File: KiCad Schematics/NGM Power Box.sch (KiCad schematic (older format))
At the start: 2 parts

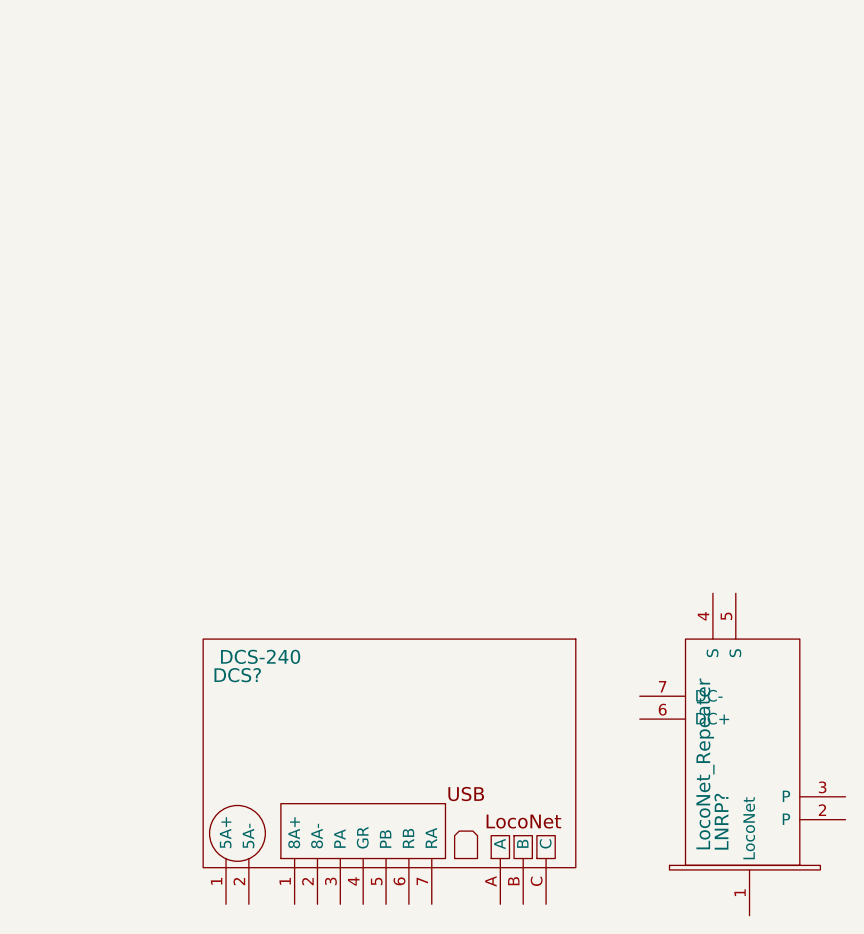
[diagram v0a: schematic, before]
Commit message: Updated schematic
Reorganized folder and updated the schematic to include multiple sheets.
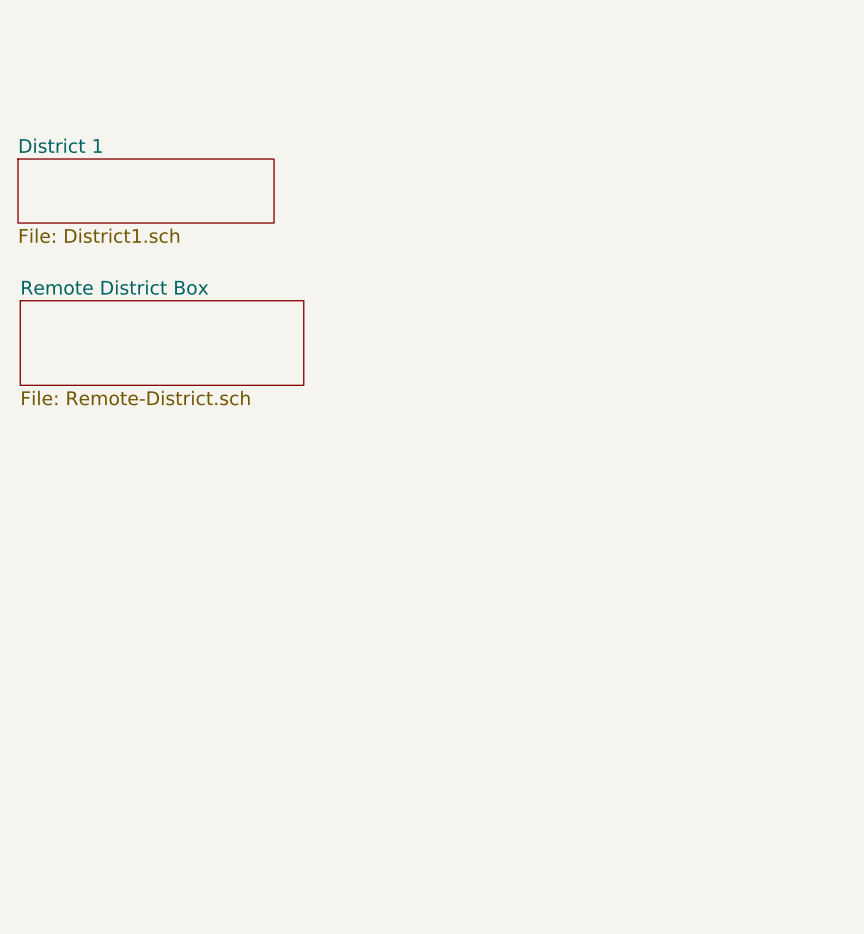
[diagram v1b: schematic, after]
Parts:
- removed DCS?: DCS-240, symbol DCS-240
- removed LNRP?: LocoNet_Repeater, symbol LocoNet_Repeater
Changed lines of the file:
@@
 EESchema Schematic File Version 2
+LIBS:NGM Power Box-rescue
 LIBS:power
 LIBS:device
@@
 LIBS:ngm_components
 LIBS:Symbols_Transformer-Diskrete_RevA
+LIBS:m-junction_box
+LIBS:NGM-Custom
+LIBS:relay_3pdt
+LIBS:NGM Power Box-cache
 EELAYER 25 0
 EELAYER END
-$Descr A4 11693 8268
+$Descr USLetter 11000 8500
 encoding utf-8
-Sheet 1 1
-Title ""
-Date ""
+Sheet 1 3
+Title "NGM Power and LocoNet Power Boxes"
+Date "2016-08-27"
 Rev ""
-Comp ""
+Comp "North Georgia Modurail"
 Comment1 ""
 Comment2 ""
@@
 Comment4 ""
 $EndDescr
-$Comp
-L DCS-240 DCS?
-U 1 1 57ACF629
-P 2100 4680
-F 0 "DCS?" H 2250 5520 60  0000 C CNN
-F 1 "DCS-240" H 2350 5600 60  0000 C CNN
-F 2 "" H 2090 4880 60  0000 C CNN
-F 3 "" H 2090 4880 60  0000 C CNN
-	1    2100 4680
-	1    0    0    -1
-$EndComp
-$Comp
-L LocoNet_Repeater LNRP?
-U 1 1 57ACF698
-P 4710 4670
-F 0 "LNRP?" H 4900 5010 60  0000 C CNN
-F 1 "LocoNet_Repeater" H 5150 5090 60  0000 C CNN
-F 2 "" H 4800 4900 60  0000 C CNN
-F 3 "" H 4800 4900 60  0000 C CNN
-	1    4710 4670
-	0    -1   -1   0
-$EndComp
+$Sheet
+S 1290 1580 1120 280
+U 57C1C4BF
+F0 "District 1" 60
+F1 "District1.sch" 60
+$EndSheet
+$Sheet
+S 1300 2200 1240 370
+U 57C1C56F
+F0 "Remote District Box" 60
+F1 "Remote-District.sch" 60
+$EndSheet
 $EndSCHEMATC

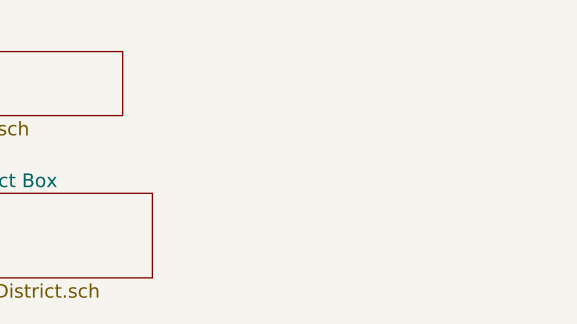
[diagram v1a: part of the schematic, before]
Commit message: Updated schematics
Fixed wiring using the correct pin-outs for the Triad transformers. Made
other minor changes.
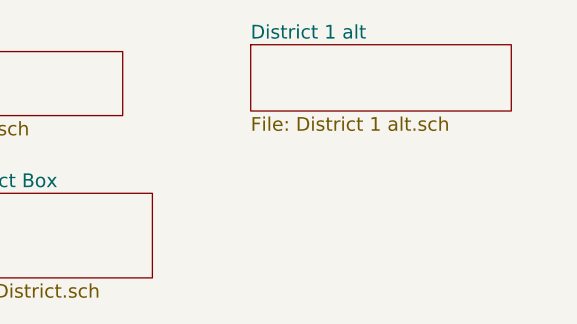
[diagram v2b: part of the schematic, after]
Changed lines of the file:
@@
 $Descr USLetter 11000 8500
 encoding utf-8
-Sheet 1 3
+Sheet 1 4
 Title "NGM Power and LocoNet Power Boxes"
 Date "2016-08-27"
-Rev ""
+Rev "2"
 Comp "North Georgia Modurail"
 Comment1 ""
@@
 F1 "Remote-District.sch" 60
 $EndSheet
+$Sheet
+S 2970 1550 1140 290
+U 57E26D35
+F0 "District 1 alt" 60
+F1 "District 1 alt.sch" 60
+$EndSheet
 $EndSCHEMATC

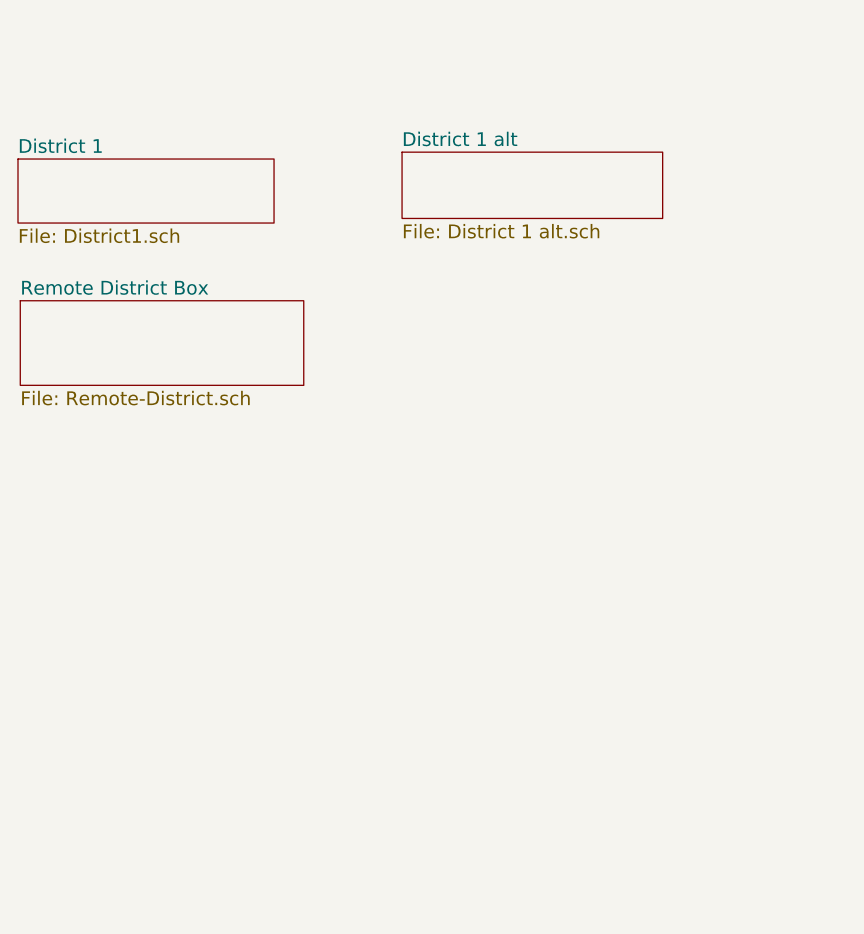
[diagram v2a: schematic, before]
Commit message: Updated schematic to include extra sheets.
Added several alternate wiring sheets and made some changes to the
schematic to reflect team decision. More to come.
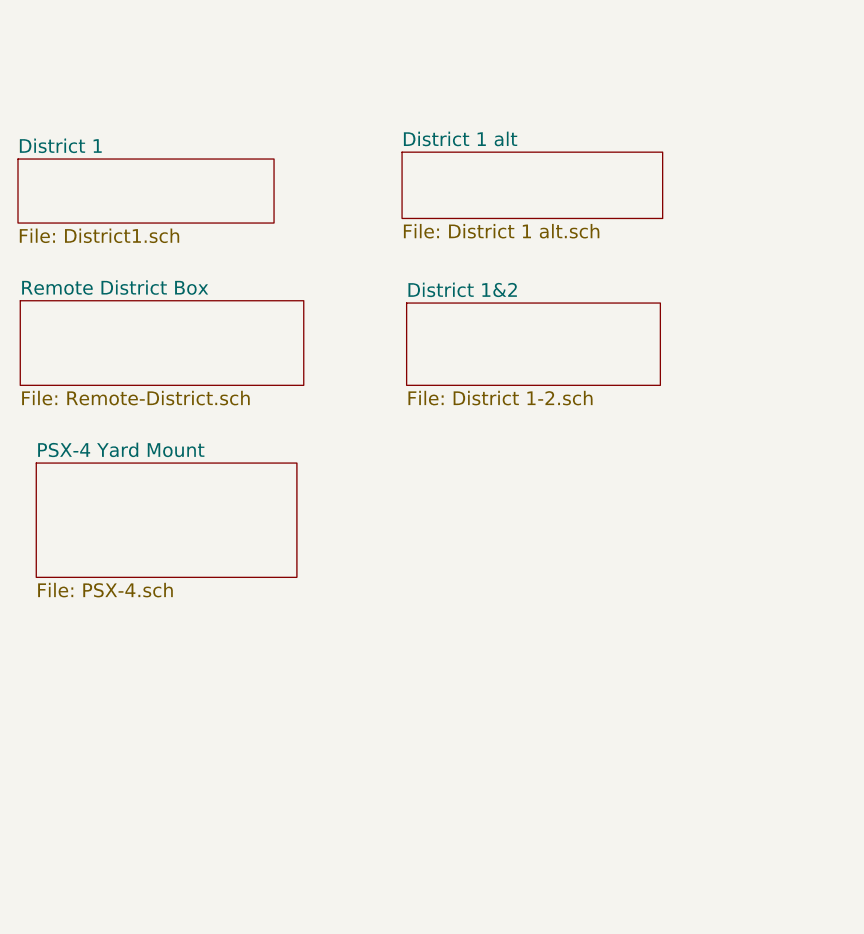
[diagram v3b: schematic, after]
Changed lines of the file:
@@
 $Descr USLetter 11000 8500
 encoding utf-8
-Sheet 1 4
+Sheet 1 6
 Title "NGM Power and LocoNet Power Boxes"
-Date "2016-08-27"
-Rev "2"
+Date "2016-09-30"
+Rev "4"
 Comp "North Georgia Modurail"
 Comment1 ""
@@
 F1 "District 1 alt.sch" 60
 $EndSheet
+$Sheet
+S 2990 2210 1110 360
+U 57EBE249
+F0 "District 1&2" 60
+F1 "District 1-2.sch" 60
+$EndSheet
+$Sheet
+S 1370 2910 1140 500
+U 57EED52C
+F0 "PSX-4 Yard Mount" 60
+F1 "PSX-4.sch" 60
+$EndSheet
 $EndSCHEMATC

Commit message: Updated schematic
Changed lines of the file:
@@
 $Descr USLetter 11000 8500
 encoding utf-8
-Sheet 1 6
+Sheet 1 7
 Title "NGM Power and LocoNet Power Boxes"
 Date "2016-09-30"
@@
 F1 "PSX-4.sch" 60
 $EndSheet
+$Sheet
+S 3220 2980 1100 390
+U 57F1B72E
+F0 "Power Box Final" 60
+F1 "Main Power Box.sch" 60
+$EndSheet
 $EndSCHEMATC

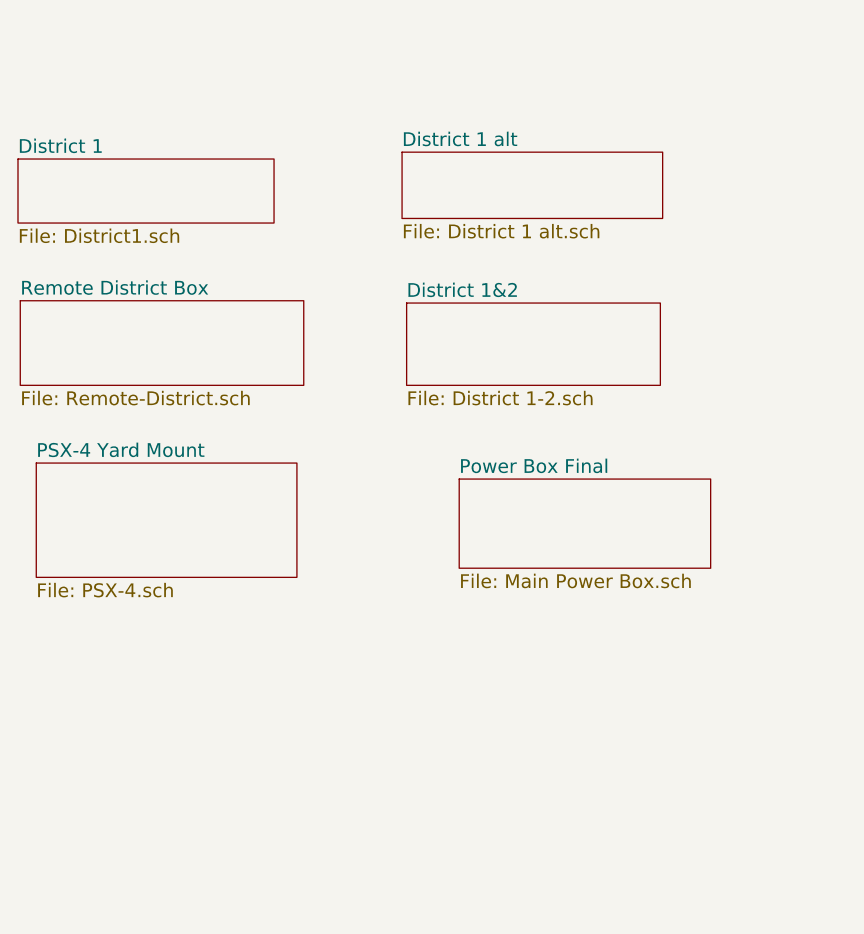
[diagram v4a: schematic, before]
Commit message: Simplified schematic
Added heirarchy sheets to simplify the schematic.
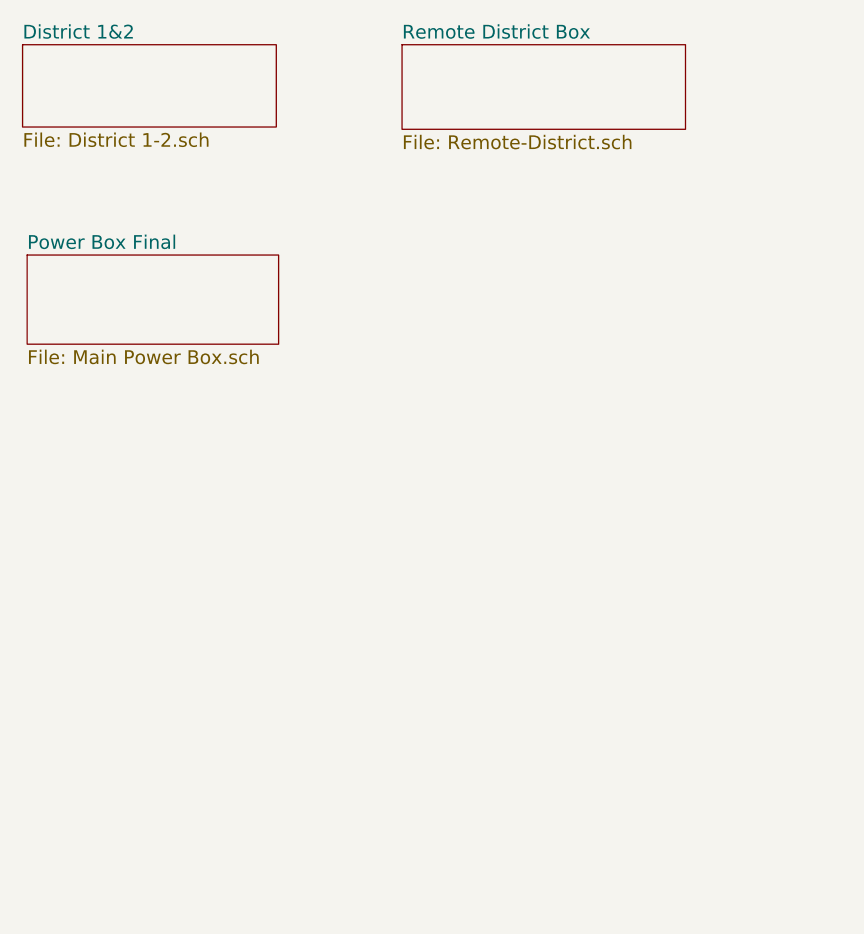
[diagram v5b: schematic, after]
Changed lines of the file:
@@
 $Descr USLetter 11000 8500
 encoding utf-8
-Sheet 1 7
+Sheet 1 16
 Title "NGM Power and LocoNet Power Boxes"
-Date "2016-09-30"
-Rev "4"
-Comp "North Georgia Modurail"
+Date "2016-10-08"
+Rev "5"
+Comp "North Georgia Modurail, Inc."
 Comment1 ""
 Comment2 ""
@@
 $EndDescr
 $Sheet
-S 1290 1580 1120 280
-U 57C1C4BF
-F0 "District 1" 60
-F1 "District1.sch" 60
-$EndSheet
-$Sheet
-S 1300 2200 1240 370
+S 2970 1080 1240 370
 U 57C1C56F
 F0 "Remote District Box" 60
@@
 $EndSheet
 $Sheet
-S 2970 1550 1140 290
-U 57E26D35
-F0 "District 1 alt" 60
-F1 "District 1 alt.sch" 60
-$EndSheet
-$Sheet
-S 2990 2210 1110 360
+S 1310 1080 1110 360
 U 57EBE249
 F0 "District 1&2" 60
@@
 $EndSheet
 $Sheet
-S 1370 2910 1140 500
-U 57EED52C
-F0 "PSX-4 Yard Mount" 60
-F1 "PSX-4.sch" 60
-$EndSheet
-$Sheet
-S 3220 2980 1100 390
+S 1330 2000 1100 390
 U 57F1B72E
 F0 "Power Box Final" 60
